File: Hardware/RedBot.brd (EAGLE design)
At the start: 94 x 49.5 mm, 39 parts, among them U2 TB6612FNG, U3 MIC5219 5V

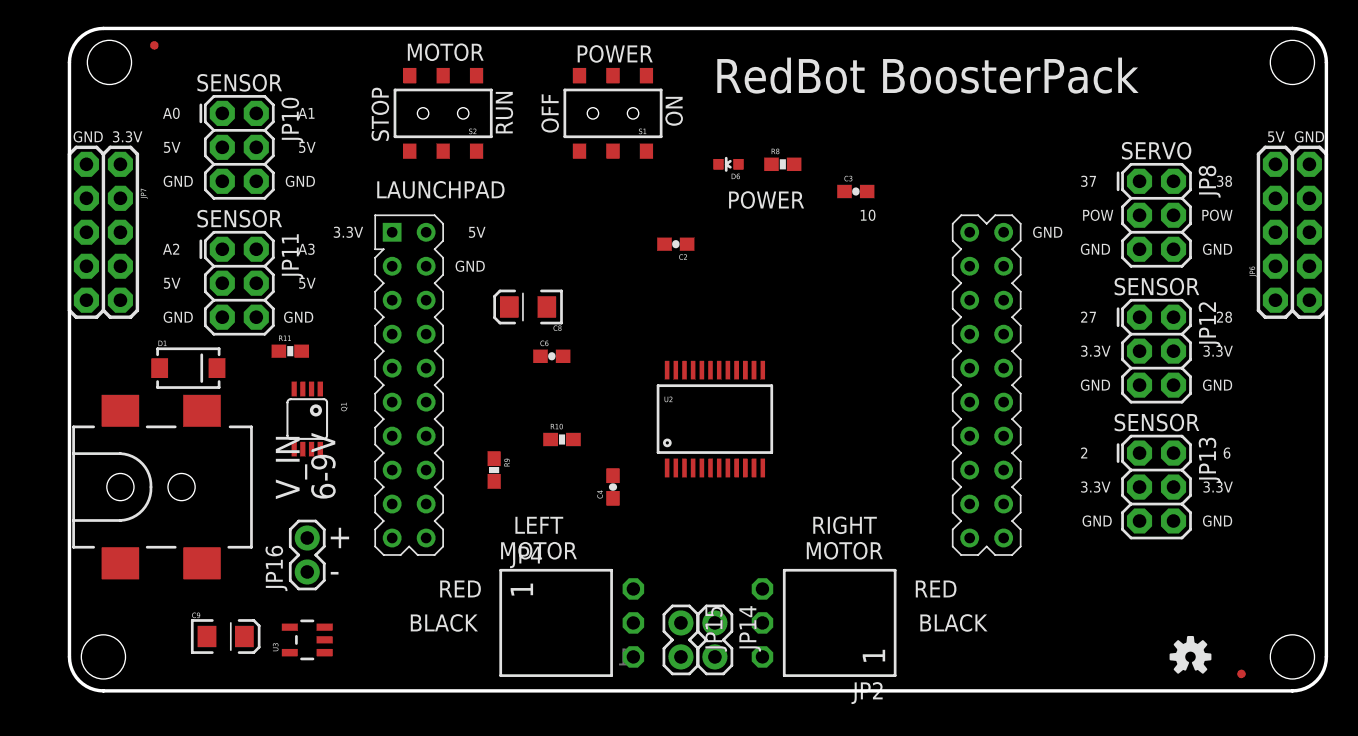
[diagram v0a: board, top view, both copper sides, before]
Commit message: Updated board with new power jack. Started routing. Added BOM
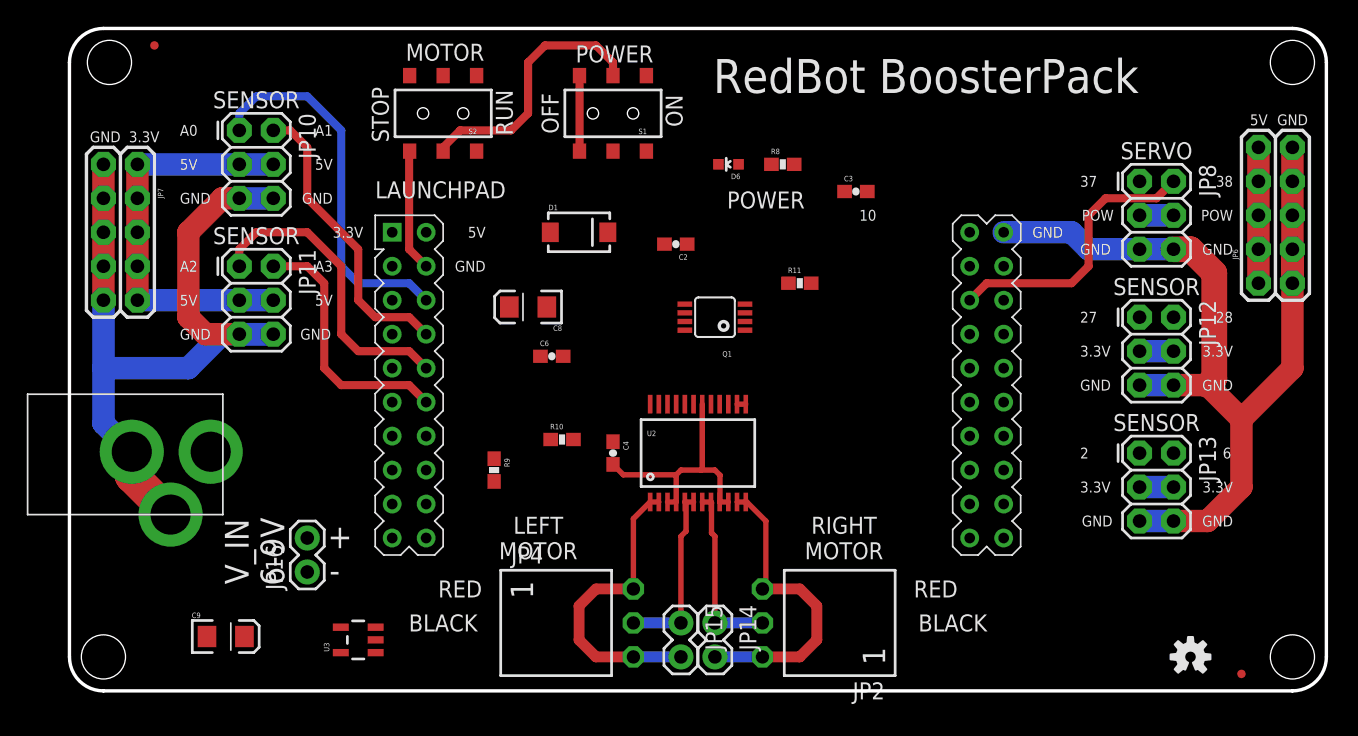
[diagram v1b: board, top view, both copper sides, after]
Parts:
- removed JP3: 5.5x2.1mm Barrel, SparkFun-Connectors:POWER_JACK_SMD
- added POWER_JACK: 2.1MMJACKTHM, adafruit:PJ-102A
- moved R11 38.4 mm to (54.6, 30.5)
- moved Q1 31.4 mm to (48.3, 27.9), turned to 90 degrees
- moved D1 30.9 mm to (38.1, 34.3)
- moved U3 3.81 mm to (21.6, 3.81)
- moved U2 2.84 mm to (47.0, 17.8)
- moved C4 2.54 mm to (40.6, 17.8), turned to 270 degrees
- moved JP10 1.80 mm to (12.7, 41.9)
- moved JP11 1.80 mm to (12.7, 31.8)
- moved JP6 1.80 mm to (90.2, 35.6)
- moved JP7 1.27 mm to (3.81, 34.3)
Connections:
- removed net PWML: U2.23
- removed net PWMR: U2.15
- net GND: now also POWER_JACK.RING, POWER_JACK.RING_SW; no longer JP3.GND, JP3.P$4
- net PWM_L: now also U2.23
- net PWM_R: now also U2.15
- net V_BATT: now also POWER_JACK.TIP; no longer JP3.VIN0
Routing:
- net GND: track 0.00 -> 168.8 mm
- net 3.3V: track 0.00 -> 35.6 mm
- net SENSOR_0: track 0.00 -> 28.0 mm
- net R01: track 0.00 -> 23.2 mm
- net SENSOR_2: track 0.00 -> 23.0 mm
- net L01: track 0.00 -> 22.9 mm
- net SENSOR_1: track 0.00 -> 22.2 mm
- net SERVO_2: track 0.00 -> 21.2 mm
- net MOTOR_ENABLE: track 0.00 -> 19.9 mm
- net SENSOR_3: track 0.00 -> 19.4 mm
- net L02: track 0.00 -> 13.4 mm
- net R02: track 0.00 -> 13.4 mm
- net 5V: track 0.00 -> 10.2 mm
- net V_GATED: track 0.00 -> 2.54 mm
- net V_BATT: track 0.00 -> 0.65 mm
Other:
- board text removed: "v1"

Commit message: Updated all parts to be larger
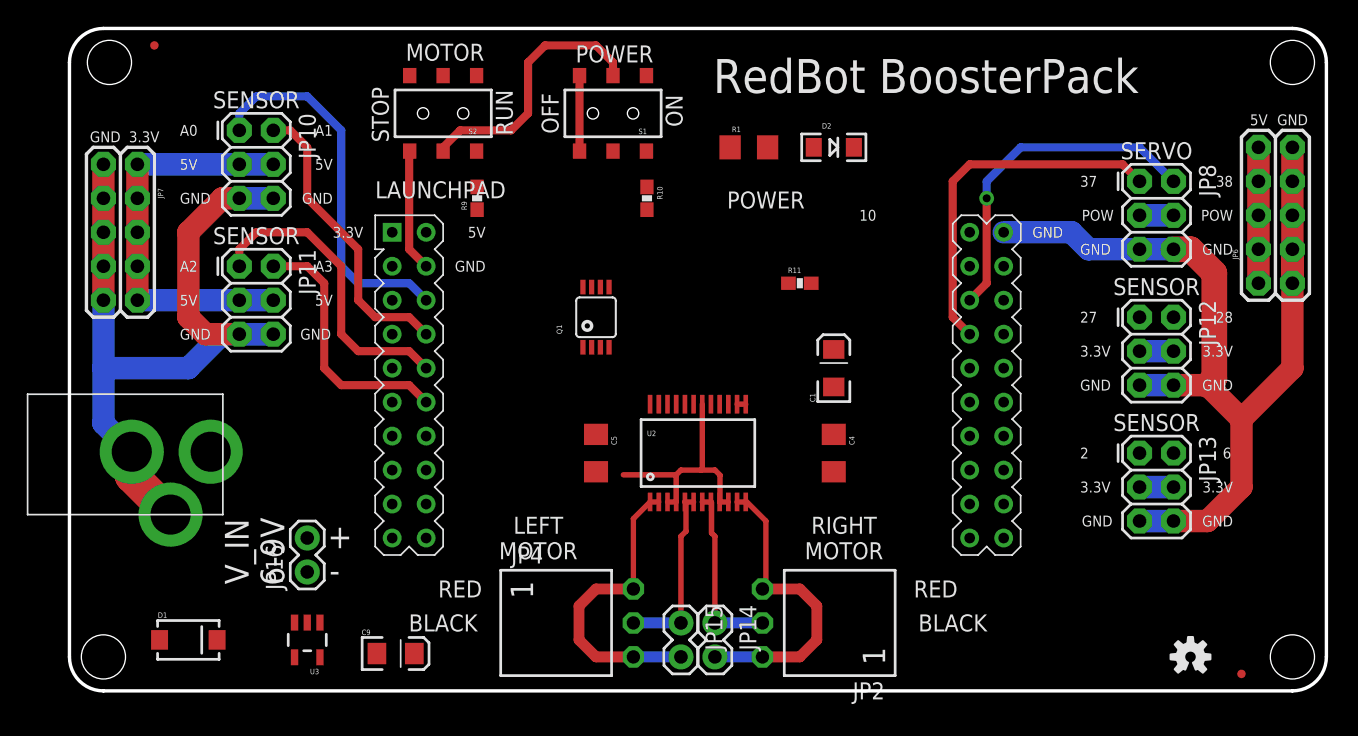
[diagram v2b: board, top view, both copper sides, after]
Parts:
- removed C2, C3, C6: 0.1uF, SparkFun-Capacitors:0603-CAP
- removed C8: 10uF, SparkFun-Capacitors:EIA3216
- removed D6: GREEN, SparkFun-LED:LED-0603
- removed R8: 1k, SparkFun-Resistors:0603-RES
- added C1: 10uF, SparkFun-Capacitors:EIA3216
- added C5: 0.1uF, SparkFun-Capacitors:1206
- added D2: GREEN, SparkFun-LED:LED-1206
- added R1: 1k, SparkFun-Resistors:1206
- C4: device SparkFun-Capacitors:0603-CAP -> SparkFun-Capacitors:1206
- moved D1 42.2 mm to (8.89, 3.81)
- moved R9 20.4 mm to (30.5, 36.8), turned to 90 degrees
- moved R10 19.1 mm to (43.2, 36.8), turned to 270 degrees
- moved C4 16.5 mm to (57.1, 17.8)
- moved C9 12.8 mm to (24.4, 2.79)
- moved Q1 8.89 mm to (39.4, 27.9), turned to 0 degrees
- moved U3 3.81 mm to (17.8, 3.81), turned to 180 degrees
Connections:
- removed net N$8: D6.A, R8.1
- new net N$1: D2.A, R1.2
- net 3.3V: now also C5.1; no longer C4.1, C6.1, C8.A
- net 5V: now also R1.1; no longer C2.1, C3.1, R8.2
- net GND: now also C1.C, C5.2, D2.C; no longer C2.2, C3.2, C6.2, C8.C, D6.C
- net V_BATT: now also C1.A, C4.1
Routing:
- net SERVO_1: track 0.00 -> 27.0 mm
- net SERVO_2: track 21.2 -> 25.5 mm, vias 0 -> 1
- net GND: track 168.8 -> 167.7 mm

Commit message: Finished layout of RedBot
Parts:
- R10, R11, R9: device SparkFun-Resistors:0603-RES -> SparkFun-Resistors:1206
- moved R11 7.41 mm to (48.3, 26.7)
- moved R9 5.68 mm to (35.6, 34.3), turned to 270 degrees
- moved C1 3.81 mm to (61.0, 24.1)
- moved Q1 2.84 mm to (38.1, 25.4)
- moved R10 2.54 mm to (43.2, 34.3)
- moved C9 2.40 mm to (23.1, 4.83), turned to 270 degrees
- moved U3 1.27 mm to (16.5, 3.81)
- moved D2 1.27 mm to (55.9, 40.6)
- moved R1 1.27 mm to (49.5, 40.6)
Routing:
- net 3.3V: track 35.6 -> 229.2 mm, vias 0 -> 6
- net GND: track 167.7 -> 347.8 mm, vias 0 -> 3
- net 5V: track 10.2 -> 137.4 mm, vias 0 -> 3
- net V_BATT: track 0.65 -> 126.3 mm, vias 0 -> 5
- net SENSOR_7: track 0.00 -> 100.8 mm, vias 0 -> 5
- net SENSOR_6: track 0.00 -> 96.6 mm, vias 0 -> 5
- net SENSOR_4: track 0.00 -> 82.1 mm, vias 0 -> 3
- net PROGRAM_ENABLE: track 0.00 -> 78.4 mm, vias 0 -> 6
- net SENSOR_5: track 0.00 -> 76.6 mm, vias 0 -> 1
- net V_IN: track 0.00 -> 58.8 mm, vias 0 -> 6
- net V_GATED: track 2.54 -> 55.4 mm, vias 0 -> 2
- net R_CTRL_2: track 0.00 -> 42.3 mm, vias 0 -> 2
- net PWM_L: track 0.00 -> 39.3 mm, vias 0 -> 3
- net L_CTRL_2: track 0.00 -> 38.4 mm, vias 0 -> 2
- net MOTOR_ENABLE: track 19.9 -> 55.8 mm
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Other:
- board text removed: "10"

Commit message: Finished silk on board
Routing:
- net SENSOR_6: track 96.6 -> 100.7 mm
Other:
- board text added: "v1.0"
